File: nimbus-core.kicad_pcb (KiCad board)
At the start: 4 copper layers, 66 x 66 mm, 71 parts, among them J1 QTE-020-03-L-D-A, J2 QSE-020-01-L-D-A, J3 532614006, J4 USB4105-GF-A-120, J5 532614006, J6 532614006, U1 STM32F405VGT7, U10 Yellow, U4 SN65HVD233-Q1, U8 SN65HVD1782-Q1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

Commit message: Place USB, add holes around PCB edge
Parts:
- moved R2 126.4 mm to (192.7, 112.0)
- moved R6 124.5 mm to (192.7, 110.0)
- moved R7 124.0 mm to (192.7, 108.0)
- moved R8 123.7 mm to (192.7, 106.0)
- moved R10 123.7 mm to (192.7, 102.0)
- moved R9 123.6 mm to (192.7, 104.0)
- moved R19 63.2 mm to (136.3, 106.4)
- moved R20 63.2 mm to (136.3, 108.1)
- moved R22 26.1 mm to (142.6, 83.5), turned to -70 degrees
- moved U9 24.2 mm to (140.8, 84.2), turned to -160 degrees
- moved R25 22.4 mm to (138.9, 84.8), turned to -70 degrees
- moved J4 22.1 mm to (139.5, 80.7), turned to -160 degrees
- moved R24 21.4 mm to (144.2, 82.9), turned to 110 degrees
- moved R23 20.6 mm to (145.7, 82.3), turned to -70 degrees
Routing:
- net /USB_VBUS: track 1.64 -> 15.8 mm
- net /I2C1_SDA: track 0.00 -> 3.85 mm, vias 0 -> 1
- net /I2C1_SCL: track 0.00 -> 3.85 mm, vias 0 -> 1
- net +3.3V: track 41.4 -> 43.6 mm, vias 9 -> 11
- net CHASSIS: vias 0 -> 60

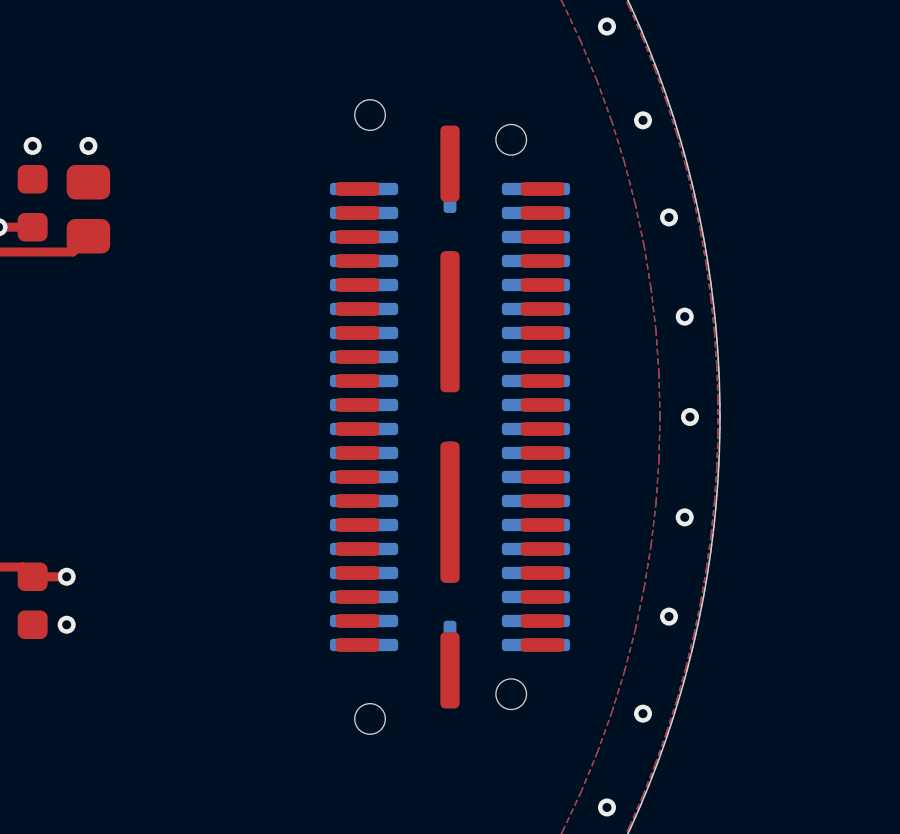
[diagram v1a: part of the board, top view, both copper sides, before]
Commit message: Connect bottom passthrough connector with top one both in schematic and PCB
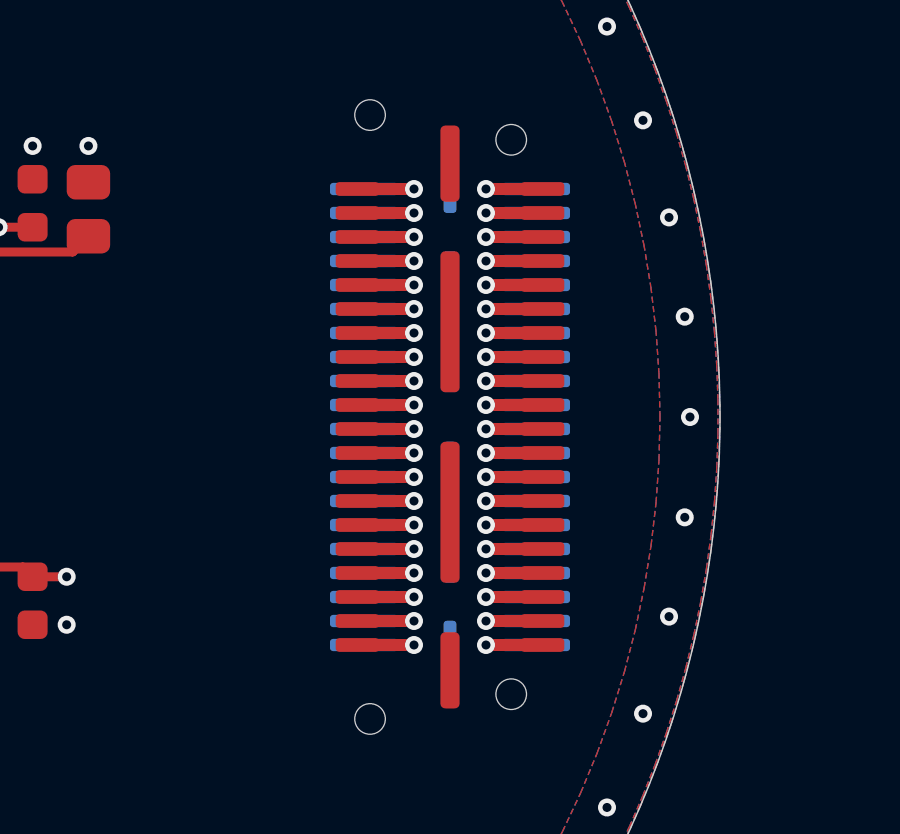
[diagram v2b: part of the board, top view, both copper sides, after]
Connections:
- J1 pad 1: unconnected-(J1-Pad1) -> /PASSTHROUGH_P1
- J1 pad 10: unconnected-(J1-Pad10) -> /PASSTHROUGH_P10
- J1 pad 11: unconnected-(J1-Pad11) -> /PASSTHROUGH_P11
- J1 pad 12: unconnected-(J1-Pad12) -> /PASSTHROUGH_P12
- J1 pad 13: unconnected-(J1-Pad13) -> /PASSTHROUGH_P13
- J1 pad 14: unconnected-(J1-Pad14) -> /PASSTHROUGH_P14
- J1 pad 15: unconnected-(J1-Pad15) -> /PASSTHROUGH_P15
- J1 pad 16: unconnected-(J1-Pad16) -> /PASSTHROUGH_P16
- J1 pad 17: unconnected-(J1-Pad17) -> /PASSTHROUGH_P17
- J1 pad 18: unconnected-(J1-Pad18) -> /PASSTHROUGH_P18
- J1 pad 19: unconnected-(J1-Pad19) -> /PASSTHROUGH_P19
- J1 pad 2: unconnected-(J1-Pad2) -> /PASSTHROUGH_P2
- J1 pad 20: unconnected-(J1-Pad20) -> /PASSTHROUGH_P20
- J1 pad 21: unconnected-(J1-Pad21) -> /PASSTHROUGH_P21
- J1 pad 22: unconnected-(J1-Pad22) -> /PASSTHROUGH_P22
- J1 pad 23: unconnected-(J1-Pad23) -> /PASSTHROUGH_P23
- J1 pad 24: unconnected-(J1-Pad24) -> /PASSTHROUGH_P24
- J1 pad 25: unconnected-(J1-Pad25) -> /PASSTHROUGH_P25
- J1 pad 26: unconnected-(J1-Pad26) -> /PASSTHROUGH_P26
- J1 pad 27: unconnected-(J1-Pad27) -> /PASSTHROUGH_P27
- J1 pad 28: unconnected-(J1-Pad28) -> /PASSTHROUGH_P28
- J1 pad 29: unconnected-(J1-Pad29) -> /PASSTHROUGH_P29
- J1 pad 3: unconnected-(J1-Pad3) -> /PASSTHROUGH_P3
- J1 pad 30: unconnected-(J1-Pad30) -> /PASSTHROUGH_P30
- J1 pad 31: unconnected-(J1-Pad31) -> /PASSTHROUGH_P31
- J1 pad 32: unconnected-(J1-Pad32) -> /PASSTHROUGH_P32
- J1 pad 33: unconnected-(J1-Pad33) -> /PASSTHROUGH_P33
- J1 pad 34: unconnected-(J1-Pad34) -> /PASSTHROUGH_P34
- J1 pad 35: unconnected-(J1-Pad35) -> /PASSTHROUGH_P35
- J1 pad 36: unconnected-(J1-Pad36) -> /PASSTHROUGH_P36
- J1 pad 37: unconnected-(J1-Pad37) -> /PASSTHROUGH_P37
- J1 pad 38: unconnected-(J1-Pad38) -> /PASSTHROUGH_P38
- J1 pad 39: unconnected-(J1-Pad39) -> /PASSTHROUGH_P39
- J1 pad 4: unconnected-(J1-Pad4) -> /PASSTHROUGH_P4
- J1 pad 40: unconnected-(J1-Pad40) -> /PASSTHROUGH_P40
- J1 pad 5: unconnected-(J1-Pad5) -> /PASSTHROUGH_P5
- J1 pad 6: unconnected-(J1-Pad6) -> /PASSTHROUGH_P6
- J1 pad 7: unconnected-(J1-Pad7) -> /PASSTHROUGH_P7
- J1 pad 8: unconnected-(J1-Pad8) -> /PASSTHROUGH_P8
- J1 pad 9: unconnected-(J1-Pad9) -> /PASSTHROUGH_P9
- J2 pad 1: unconnected-(J2-Pad1) -> /PASSTHROUGH_P1
- J2 pad 10: unconnected-(J2-Pad10) -> /PASSTHROUGH_P10
- J2 pad 11: unconnected-(J2-Pad11) -> /PASSTHROUGH_P11
- J2 pad 12: unconnected-(J2-Pad12) -> /PASSTHROUGH_P12
- J2 pad 13: unconnected-(J2-Pad13) -> /PASSTHROUGH_P13
- J2 pad 14: unconnected-(J2-Pad14) -> /PASSTHROUGH_P14
- J2 pad 15: unconnected-(J2-Pad15) -> /PASSTHROUGH_P15
- J2 pad 16: unconnected-(J2-Pad16) -> /PASSTHROUGH_P16
- J2 pad 17: unconnected-(J2-Pad17) -> /PASSTHROUGH_P17
- J2 pad 18: unconnected-(J2-Pad18) -> /PASSTHROUGH_P18
- J2 pad 19: unconnected-(J2-Pad19) -> /PASSTHROUGH_P19
- J2 pad 2: unconnected-(J2-Pad2) -> /PASSTHROUGH_P2
- J2 pad 20: unconnected-(J2-Pad20) -> /PASSTHROUGH_P20
- J2 pad 21: unconnected-(J2-Pad21) -> /PASSTHROUGH_P21
- J2 pad 22: unconnected-(J2-Pad22) -> /PASSTHROUGH_P22
- J2 pad 23: unconnected-(J2-Pad23) -> /PASSTHROUGH_P23
- J2 pad 24: unconnected-(J2-Pad24) -> /PASSTHROUGH_P24
- J2 pad 25: unconnected-(J2-Pad25) -> /PASSTHROUGH_P25
- J2 pad 26: unconnected-(J2-Pad26) -> /PASSTHROUGH_P26
- J2 pad 27: unconnected-(J2-Pad27) -> /PASSTHROUGH_P27
- J2 pad 28: unconnected-(J2-Pad28) -> /PASSTHROUGH_P28
- J2 pad 29: unconnected-(J2-Pad29) -> /PASSTHROUGH_P29
- J2 pad 3: unconnected-(J2-Pad3) -> /PASSTHROUGH_P3
- J2 pad 30: unconnected-(J2-Pad30) -> /PASSTHROUGH_P30
- J2 pad 31: unconnected-(J2-Pad31) -> /PASSTHROUGH_P31
- J2 pad 32: unconnected-(J2-Pad32) -> /PASSTHROUGH_P32
- J2 pad 33: unconnected-(J2-Pad33) -> /PASSTHROUGH_P33
- J2 pad 34: unconnected-(J2-Pad34) -> /PASSTHROUGH_P34
- J2 pad 35: unconnected-(J2-Pad35) -> /PASSTHROUGH_P35
- J2 pad 36: unconnected-(J2-Pad36) -> /PASSTHROUGH_P36
- J2 pad 37: unconnected-(J2-Pad37) -> /PASSTHROUGH_P37
- J2 pad 38: unconnected-(J2-Pad38) -> /PASSTHROUGH_P38
- J2 pad 39: unconnected-(J2-Pad39) -> /PASSTHROUGH_P39
- J2 pad 4: unconnected-(J2-Pad4) -> /PASSTHROUGH_P4
- J2 pad 40: unconnected-(J2-Pad40) -> /PASSTHROUGH_P40
- J2 pad 5: unconnected-(J2-Pad5) -> /PASSTHROUGH_P5
- J2 pad 6: unconnected-(J2-Pad6) -> /PASSTHROUGH_P6
- J2 pad 7: unconnected-(J2-Pad7) -> /PASSTHROUGH_P7
- J2 pad 8: unconnected-(J2-Pad8) -> /PASSTHROUGH_P8
- J2 pad 9: unconnected-(J2-Pad9) -> /PASSTHROUGH_P9
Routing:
- net /PASSTHROUGH_P9: track 0.00 -> 3.55 mm, vias 0 -> 1
- net /PASSTHROUGH_P8: track 0.00 -> 3.55 mm, vias 0 -> 1
- net /PASSTHROUGH_P7: track 0.00 -> 3.55 mm, vias 0 -> 1
- net /PASSTHROUGH_P6: track 0.00 -> 3.55 mm, vias 0 -> 1
- net /PASSTHROUGH_P5: track 0.00 -> 3.55 mm, vias 0 -> 1
- net /PASSTHROUGH_P40: track 0.00 -> 3.55 mm, vias 0 -> 1
- net /PASSTHROUGH_P4: track 0.00 -> 3.55 mm, vias 0 -> 1
- net /PASSTHROUGH_P39: track 0.00 -> 3.55 mm, vias 0 -> 1
- net /PASSTHROUGH_P38: track 0.00 -> 3.55 mm, vias 0 -> 1
- net /PASSTHROUGH_P37: track 0.00 -> 3.55 mm, vias 0 -> 1
- net /PASSTHROUGH_P36: track 0.00 -> 3.55 mm, vias 0 -> 1
- net /PASSTHROUGH_P35: track 0.00 -> 3.55 mm, vias 0 -> 1
- net /PASSTHROUGH_P34: track 0.00 -> 3.55 mm, vias 0 -> 1
- net /PASSTHROUGH_P33: track 0.00 -> 3.55 mm, vias 0 -> 1
- net /PASSTHROUGH_P32: track 0.00 -> 3.55 mm, vias 0 -> 1
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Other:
- board text added: "J2"
